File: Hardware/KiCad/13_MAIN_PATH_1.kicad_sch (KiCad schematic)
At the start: 0 parts

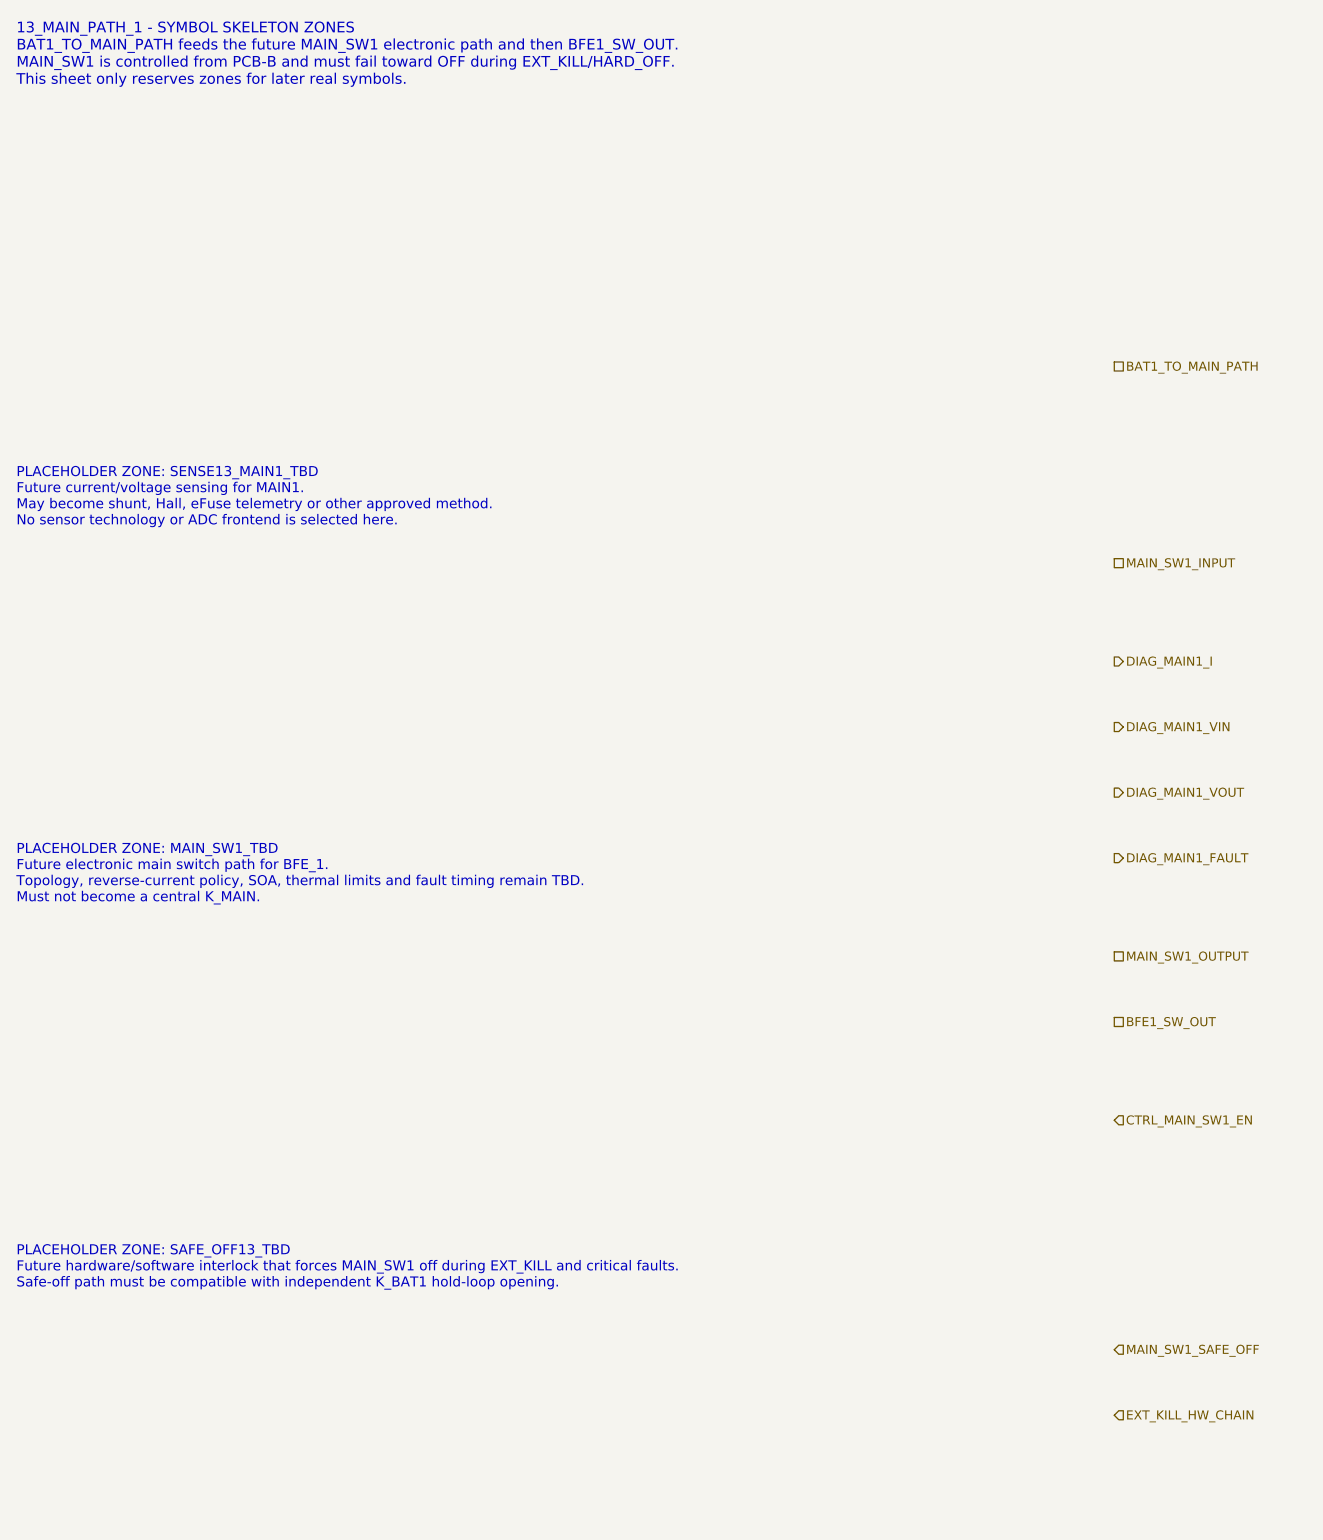
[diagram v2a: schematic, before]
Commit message: hardware: align PCB-A main path 1 control interface
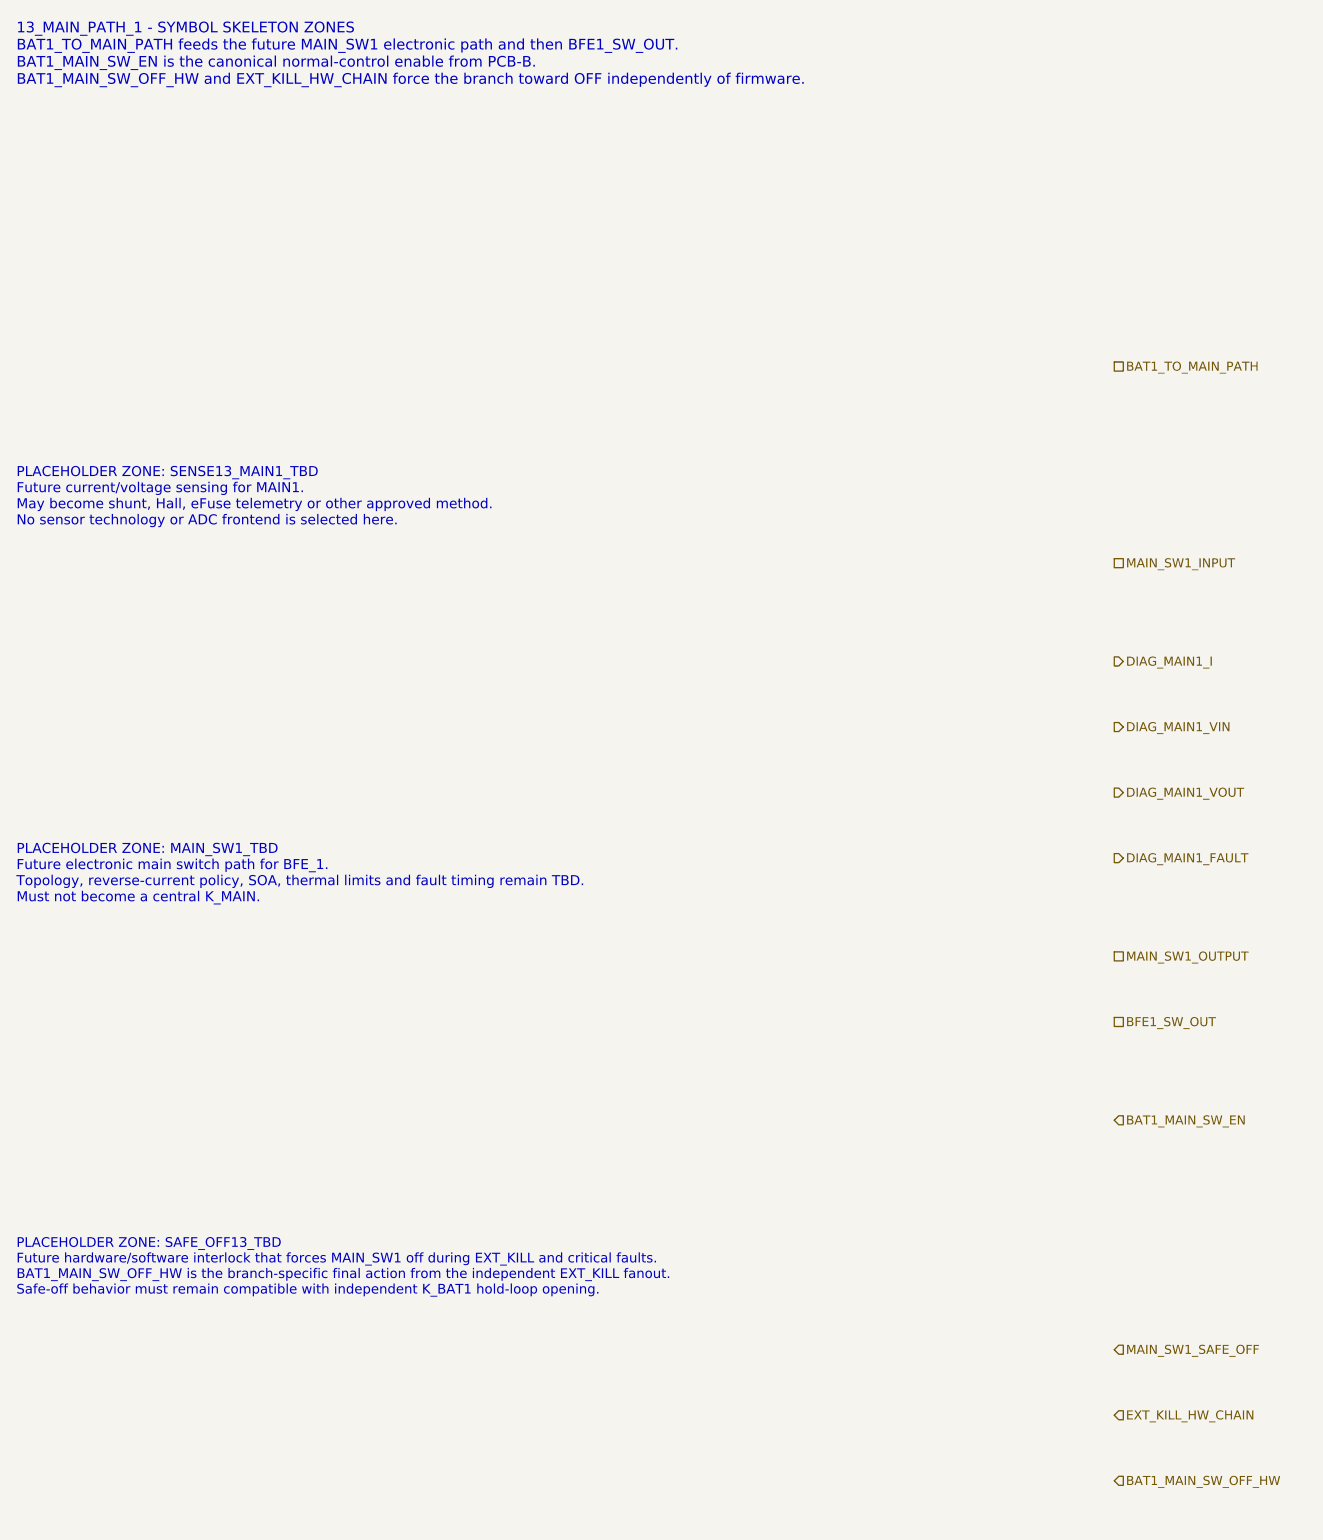
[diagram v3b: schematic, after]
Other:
- note added: "13_MAIN_PATH_1 - SYMBOL SKELETON ZONES BAT1_TO_MAIN_PATH feeds the future MAIN_SW1 electronic path and then BFE1_SW_OUT. BAT1_MAIN_SW_EN is the canonical normal-control enable from PCB-B. BAT1_MAIN_SW_OFF_HW and EXT_KILL_HW_CHAIN force the branch toward OFF independently of firmware."
- note added: "PLACEHOLDER ZONE: SAFE_OFF13_TBD Future hardware/software interlock that forces MAIN_SW1 off during EXT_KILL and critical faults. BAT1_MAIN_SW_OFF_HW is the branch-specific final action from the independent EXT_KILL fanout. Safe-off behavior must remain compatible with independent K_BAT1 hold-loop opening."
- note removed: "13_MAIN_PATH_1 - SYMBOL SKELETON ZONES BAT1_TO_MAIN_PATH feeds the future MAIN_SW1 electronic path and then BFE1_SW_OUT. MAIN_SW1 is controlled from PCB-B and must fail toward OFF during EXT_KILL/HARD_OFF. This sheet only reserves zones for later real symbols."
- note removed: "PLACEHOLDER ZONE: SAFE_OFF13_TBD Future hardware/software interlock that forces MAIN_SW1 off during EXT_KILL and critical faults. Safe-off path must be compatible with independent K_BAT1 hold-loop opening."
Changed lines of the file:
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@@
 		(title "13_MAIN_PATH_1 - BFE_1 main electronic path")
 		(date "2026-07-15")
-		(rev "C1")
+		(rev "C2")
 		(company "Gonoboben/plataVM")
-		(comment 1 "Symbol skeleton: MAIN_SW1, sensing and safe-off placeholders")
+		(comment 1 "Interface consistency: canonical BAT1 main-switch control and hardware-off boundaries")
 		(comment 2 "No MOSFET, eFuse, ideal-diode, current sensor or footprint selected")
 	)
-	(text "13_MAIN_PATH_1 - SYMBOL SKELETON ZONES\nBAT1_TO_MAIN_PATH feeds the future MAIN_SW1 electronic path and then BFE1_SW_OUT.\nMAIN_SW1 is controlled from PCB-B and must fail toward OFF during EXT_KILL/HARD_OFF.\nThis sheet only reserves zones for later real symbols."
+	(text "13_MAIN_PATH_1 - SYMBOL SKELETON ZONES\nBAT1_TO_MAIN_PATH feeds the future MAIN_SW1 electronic path and then BFE1_SW_OUT.\nBAT1_MAIN_SW_EN is the canonical normal-control enable from PCB-B.\nBAT1_MAIN_SW_OFF_HW and EXT_KILL_HW_CHAIN force the branch toward OFF independently of firmware."
 		(exclude_from_sim no)
 		(at 12 16 0)
@@
 		(uuid "bfe-lb-00000013-0000-4000-8000-000000000103")
 	)
-	(text "PLACEHOLDER ZONE: SAFE_OFF13_TBD\nFuture hardware/software interlock that forces MAIN_SW1 off during EXT_KILL and critical faults.\nSafe-off path must be compatible with independent K_BAT1 hold-loop opening."
+	(text "PLACEHOLDER ZONE: SAFE_OFF13_TBD\nFuture hardware/software interlock that forces MAIN_SW1 off during EXT_KILL and critical faults.\nBAT1_MAIN_SW_OFF_HW is the branch-specific final action from the independent EXT_KILL fanout.\nSafe-off behavior must remain compatible with independent K_BAT1 hold-loop opening."
 		(exclude_from_sim no)
 		(at 12 164 0)
-		(effects (font (size 1.22 1.22)) (justify left))
+		(effects (font (size 1.18 1.18)) (justify left))
 		(uuid "bfe-lb-00000013-0000-4000-8000-000000000104")
 	)
@@
 	(hierarchical_label "MAIN_SW1_OUTPUT" (shape passive) (exclude_from_sim no) (at 146 126 0) (effects (font (size 1.1 1.1)) (justify left)) (uuid "bfe-lb-00000013-0000-4000-8000-000000000203"))
 	(hierarchical_label "BFE1_SW_OUT" (shape passive) (exclude_from_sim no) (at 146 134 0) (effects (font (size 1.1 1.1)) (justify left)) (uuid "bfe-lb-00000013-0000-4000-8000-000000000204"))
-	(hierarchical_label "CTRL_MAIN_SW1_EN" (shape input) (exclude_from_sim no) (at 146 146 0) (effects (font (size 1.1 1.1)) (justify left)) (uuid "bfe-lb-00000013-0000-4000-8000-000000000205"))
+	(hierarchical_label "BAT1_MAIN_SW_EN" (shape input) (exclude_from_sim no) (at 146 146 0) (effects (font (size 1.1 1.1)) (justify left)) (uuid "bfe-lb-00000013-0000-4000-8000-000000000205"))
 	(hierarchical_label "MAIN_SW1_SAFE_OFF" (shape input) (exclude_from_sim no) (at 146 174 0) (effects (font (size 1.1 1.1)) (justify left)) (uuid "bfe-lb-00000013-0000-4000-8000-000000000206"))
 	(hierarchical_label "EXT_KILL_HW_CHAIN" (shape input) (exclude_from_sim no) (at 146 182 0) (effects (font (size 1.1 1.1)) (justify left)) (uuid "bfe-lb-00000013-0000-4000-8000-000000000207"))
+	(hierarchical_label "BAT1_MAIN_SW_OFF_HW" (shape input) (exclude_from_sim no) (at 146 190 0) (effects (font (size 1.1 1.1)) (justify left)) (uuid "bfe-lb-00000013-0000-4000-8000-000000000212"))
 	(hierarchical_label "DIAG_MAIN1_I" (shape output) (exclude_from_sim no) (at 146 90 0) (effects (font (size 1.1 1.1)) (justify left)) (uuid "bfe-lb-00000013-0000-4000-8000-000000000208"))
 	(hierarchical_label "DIAG_MAIN1_VIN" (shape output) (exclude_from_sim no) (at 146 98 0) (effects (font (size 1.1 1.1)) (justify left)) (uuid "bfe-lb-00000013-0000-4000-8000-000000000209"))
